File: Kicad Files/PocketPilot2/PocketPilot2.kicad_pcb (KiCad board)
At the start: 2 copper layers, 57.9 x 85.3 mm, 33 parts, among them P1 Conn_02x18_Odd_Even, P2 Conn_02x18_Odd_Even, Q1 BC548, U1 GY-912

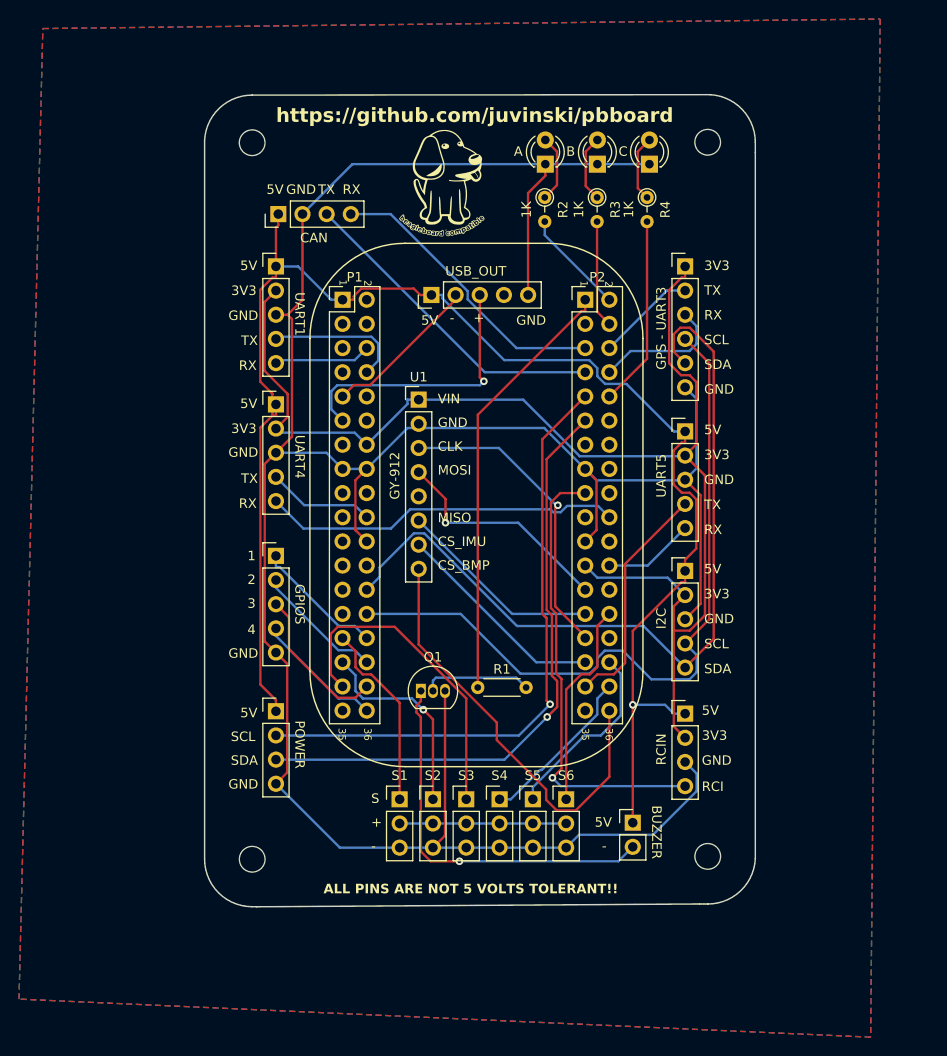
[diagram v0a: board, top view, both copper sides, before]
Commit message: Update to version to 1.1 Update GPIO pins
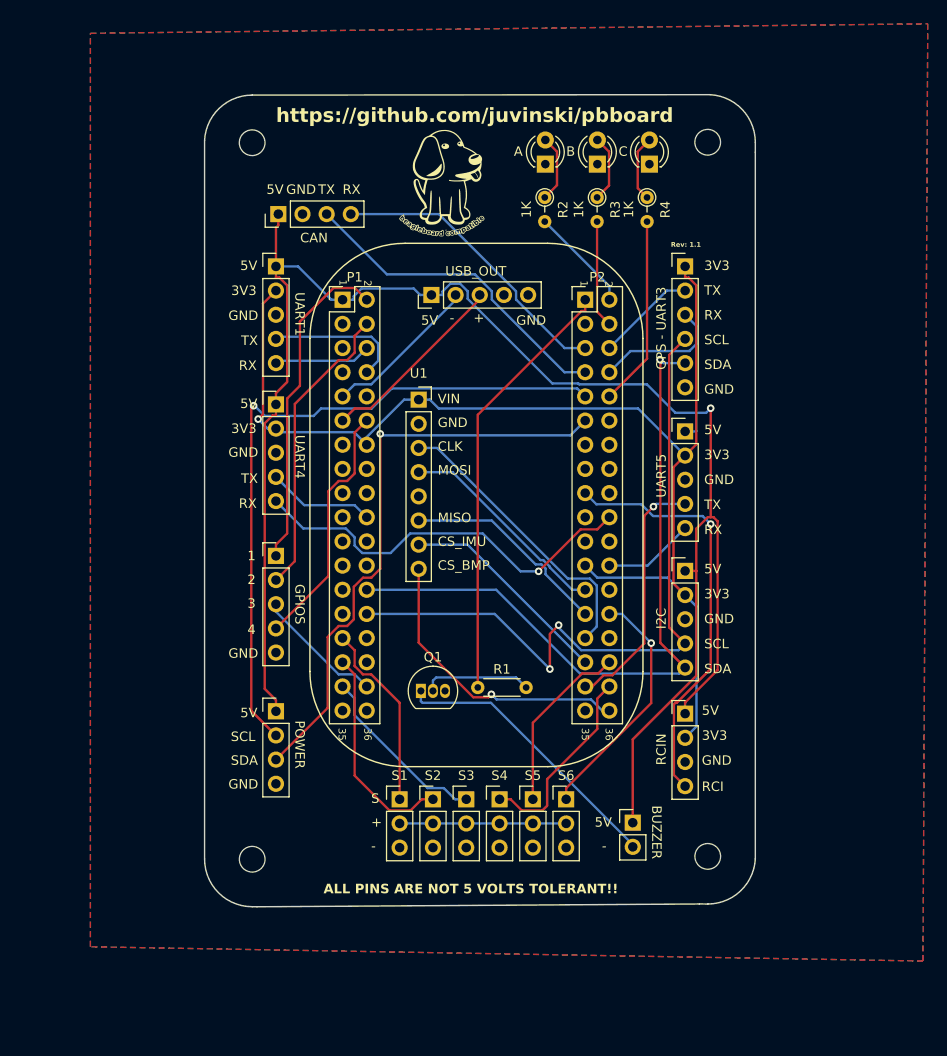
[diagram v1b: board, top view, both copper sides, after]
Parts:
- U1: footprint Connector_PinHeader_2.54mm:PinHeader_1x08_P2.54mm_Vertical -> Connector_PinSocket_2.54mm:PinSocket_1x08_P2.54mm_Vertical
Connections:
- P1 pad 12: unconnected-(P1-Pin_12-Pad12) -> /GPIO4
- P1 pad 2: unconnected-(P1-Pin_2-Pad2) -> /GPIO1
- P1 pad 30: /GPIO1 -> unconnected-(P1-Pin_30-Pad30)
- P1 pad 32: /GPIO2 -> unconnected-(P1-Pin_32-Pad32)
- P1 pad 36: /GPIO4 -> unconnected-(P1-Pin_36-Pad36)
- P1 pad 4: unconnected-(P1-Pin_4-Pad4) -> /GPIO2
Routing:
- net GND: track 279.9 -> 0.00 mm
- net +5V: track 160.8 -> 183.8 mm
- net /GPIO1: track 13.8 -> 34.7 mm
- net /GPIO2: track 13.6 -> 31.4 mm
- net /OUT3: track 34.3 -> 18.9 mm
- net /SPI_CS1: track 45.4 -> 31.0 mm, vias 0 -> 1
- net /GPIO4: track 13.6 -> 26.3 mm
- net /I2C_SDA: track 85.8 -> 73.6 mm, vias 0 -> 1
- net Net-(O15-Pin_2): track 40.6 -> 29.8 mm, vias 1 -> 0
- net /USB_POS: track 29.3 -> 20.2 mm, vias 1 -> 0
- net +3.3V: track 137.3 -> 129.4 mm, vias 0 -> 1
- net /I2C3_SCL: track 65.0 -> 72.7 mm
- net /UART4_RX: track 38.0 -> 42.7 mm, vias 0 -> 1
- net /OUT6: track 21.9 -> 25.8 mm, vias 0 -> 1
- net /RC_INPUT: track 48.1 -> 44.2 mm
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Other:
- board text added: "Rev: 1.1"

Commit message: Version 1.2 release 	Update board to add analog power sensing. 	Update images and instructions.
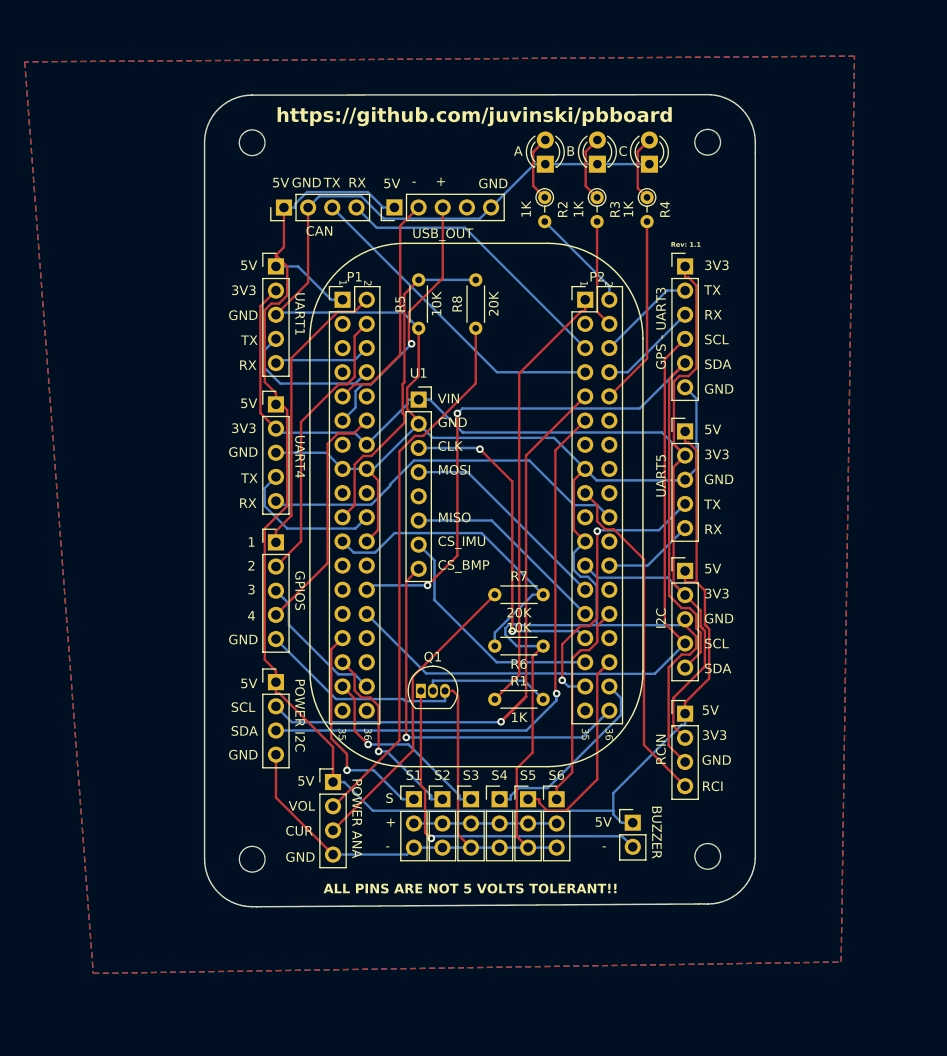
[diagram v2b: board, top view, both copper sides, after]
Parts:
- removed G***: LOGO, Logos:beagle_compatible_10x10
- added O14: POWER ANALOG, Connector_PinHeader_2.54mm:PinHeader_1x04_P2.54mm_Vertical, F.Cu at (126.0, 134.7)
- added R5: 10K, Resistor_THT:R_Axial_DIN0204_L3.6mm_D1.6mm_P5.08mm_Horizontal, F.Cu at (135.0, 87.0)
- added R6: 10K, Resistor_THT:R_Axial_DIN0204_L3.6mm_D1.6mm_P5.08mm_Horizontal, F.Cu at (148.1, 120.4)
- added R7: 20K, Resistor_THT:R_Axial_DIN0204_L3.6mm_D1.6mm_P5.08mm_Horizontal, F.Cu at (143.0, 115.0)
- added R8: 20K, Resistor_THT:R_Axial_DIN0204_L3.6mm_D1.6mm_P5.08mm_Horizontal, F.Cu at (141.0, 87.0)
- O16: value POWER -> POWER I2C
- moved O18 9.99 mm to (132.4, 74.3)
- moved O16 3.06 mm to (120.0, 124.2)
- moved R1 2.18 mm to (143.0, 126.0)
- moved O1 1.50 mm to (134.5, 136.5)
- moved O17 1.42 mm to (120.0, 109.5)
- moved O2 1.00 mm to (137.5, 136.5)
- moved O6 1.00 mm to (149.5, 136.5)
- moved O7 0.91 mm to (120.8, 74.3)
- moved O3 0.50 mm to (140.5, 136.5)
- moved O5 0.50 mm to (146.5, 136.5)
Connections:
- P1 pad 19: unconnected-(P1-Pin_19-Pad19) -> /VOLTAGE
- P1 pad 21: unconnected-(P1-Pin_21-Pad21) -> /CURRENT
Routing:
- net GND: track 0.00 -> 308.4 mm
- net Net-(O14-Pin_2): track 0.00 -> 57.0 mm
- net /VOLTAGE: track 0.00 -> 35.2 mm
- net /CURRENT: track 0.00 -> 33.2 mm
- net Net-(O14-Pin_3): track 0.00 -> 31.8 mm
- net /I2C_SDA: track 73.6 -> 87.3 mm, vias 1 -> 2
- net +5V: track 183.8 -> 172.8 mm, vias 1 -> 0
- net /SPI_CS1: track 31.0 -> 40.8 mm
- net Net-(O15-Pin_2): track 29.8 -> 39.5 mm, vias 0 -> 1
- net /RC_INPUT: track 44.2 -> 35.7 mm, vias 1 -> 0
- net /USB_NEG: track 16.6 -> 24.2 mm
- net /USB_POS: track 20.2 -> 27.5 mm, vias 0 -> 1
- net /UART5_TX: track 26.3 -> 30.8 mm, vias 1 -> 2
- net /UART4_TX: track 11.3 -> 15.8 mm
- net /SPI_CLK: track 30.7 -> 35.0 mm, vias 0 -> 2
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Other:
- board text added: "CUR"
- board text added: "POWER ANA"
- board text added: "VOL"
